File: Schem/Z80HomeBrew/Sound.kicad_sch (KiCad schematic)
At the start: 16 parts, among them J6 AudioJack3, U11 74HC00, U13 LM386, U18 SN76489AN, U8 SN76489AN, U9 74HC00

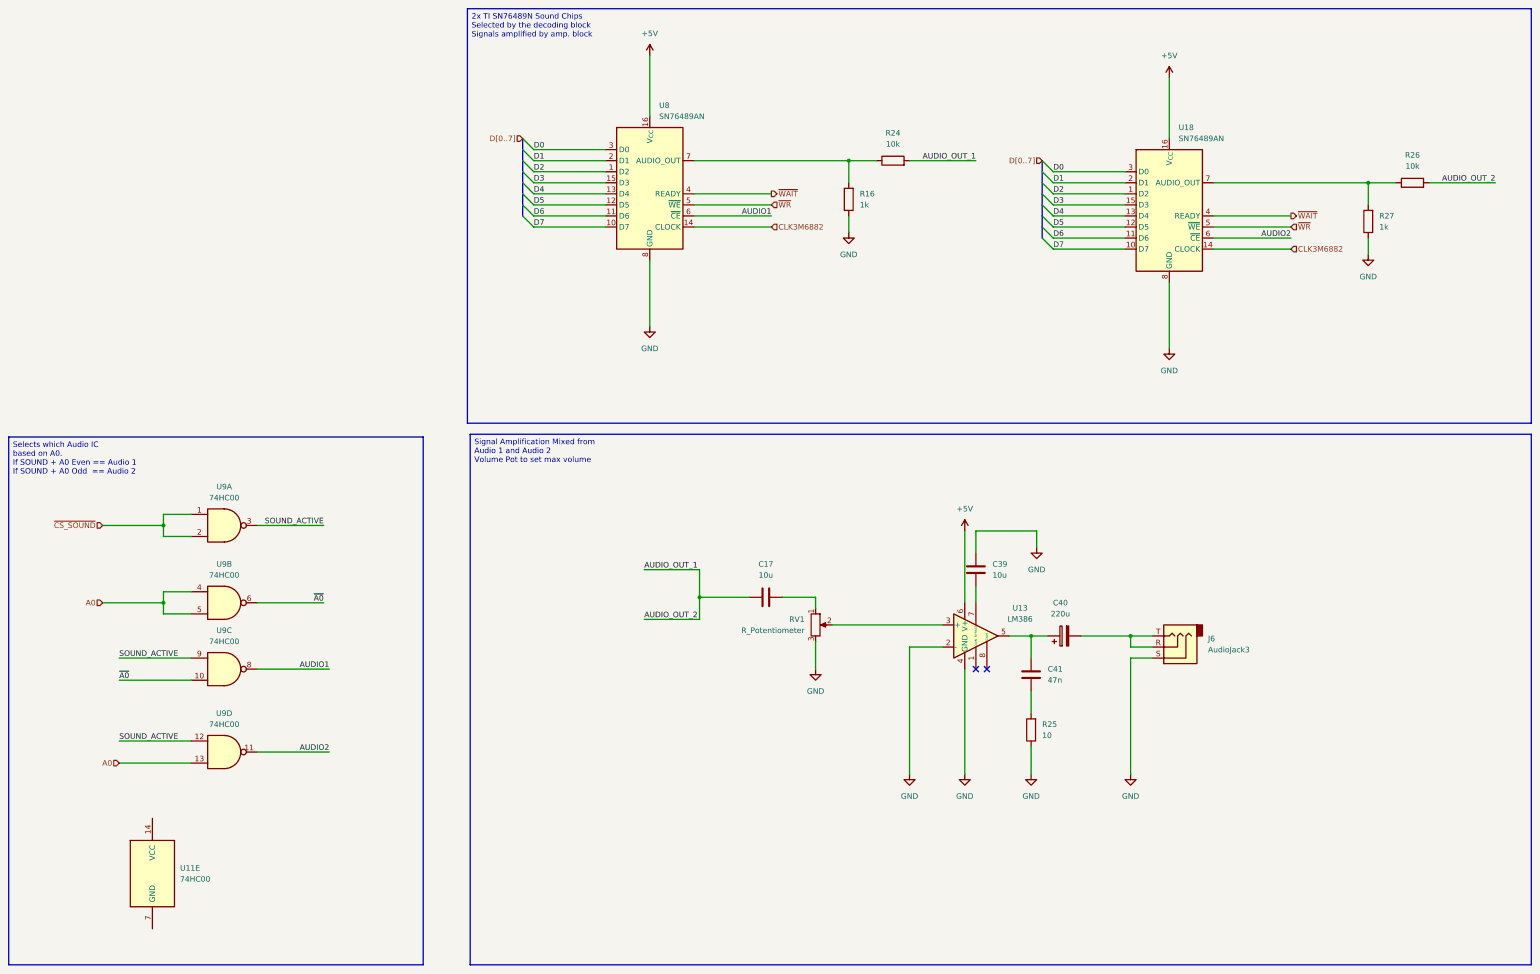
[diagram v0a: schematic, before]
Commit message: Video block added. fixed some issues with parts...
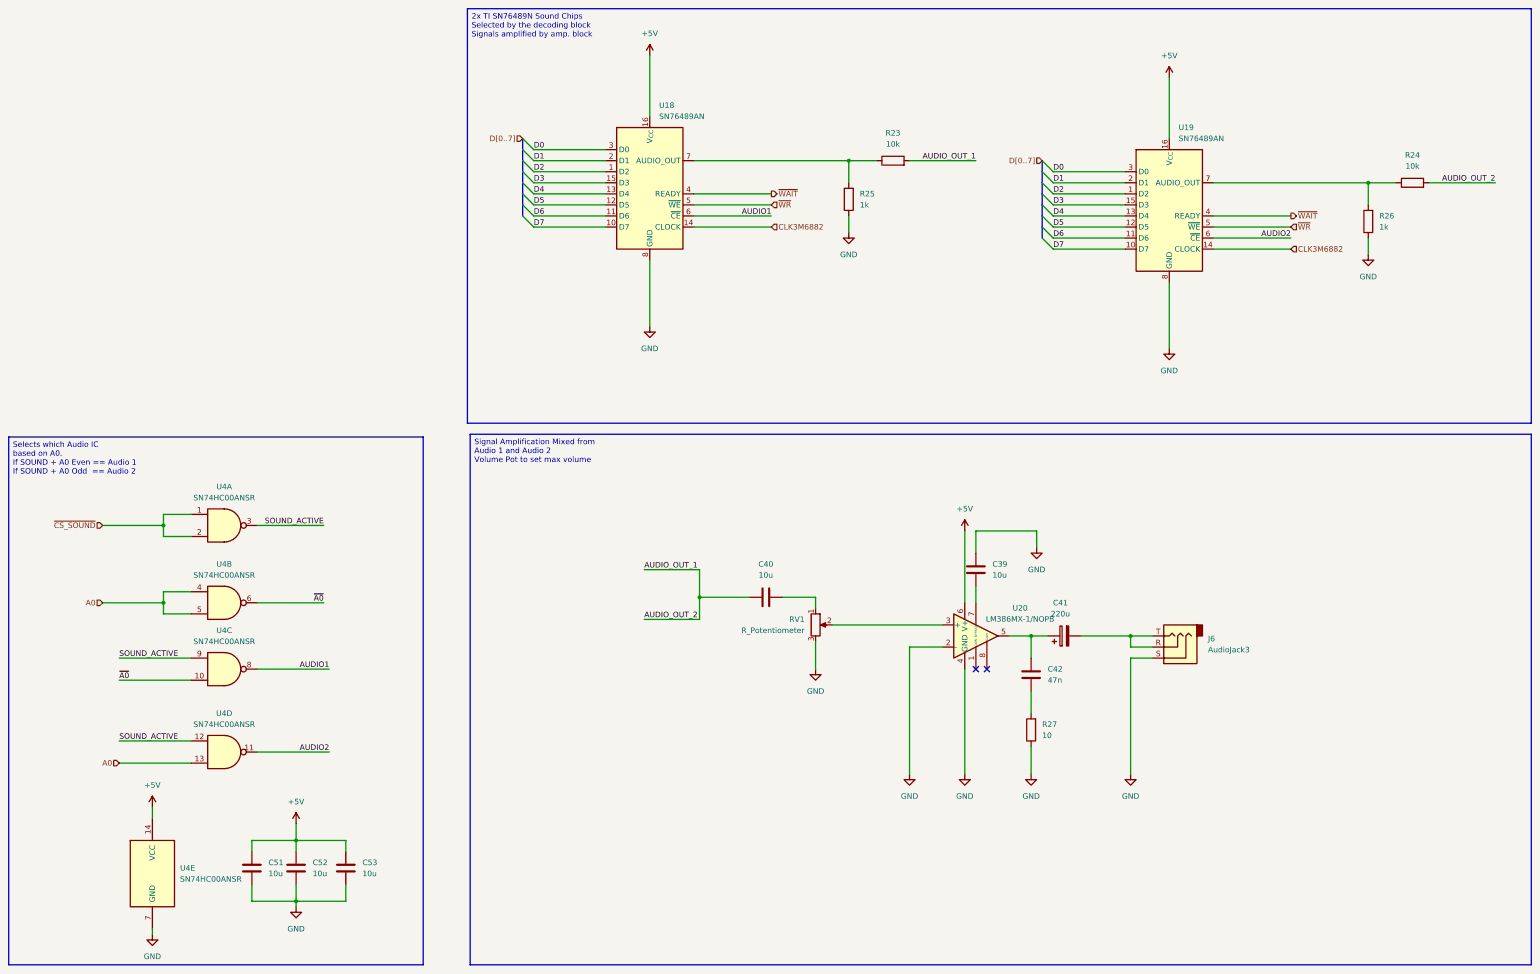
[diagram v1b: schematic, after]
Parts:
- added C51, C52, C53: 10u, Capacitor_SMD:C_1206_3216Metric, symbol Device:C
- U20: renamed from U13; value LM386 -> LM386MX-1/NOPB; footprint (none) -> Package_SO:SOIC-8_3.9x4.9mm_P1.27mm
- U4: renamed from U9; value 74HC00 -> SN74HC00ANSR; footprint (none) -> Footprints:SO14NB_TEX
- U4: renamed from U11; value 74HC00 -> SN74HC00ANSR; footprint (none) -> Footprints:SO14NB_TEX
- renumbered C17 to C40, C40 to C41, C41 to C42, R24 to R23, R26 to R24, R16 to R25, R27 to R26, R25 to R27, U8 to U18, U18 to U19
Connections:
- net +5V: now also U4.14 (VCC), C51.2, C52.2, C53.2
- net GND: now also U4.7 (GND), C51.1, C52.1, C53.1

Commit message: Completed schematics
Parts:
- J6: value AudioJack3 -> STX-3120-3B; footprint Connector_Audio:Jack_3.5mm_CUI_SJ1-3523N_Horizontal -> Footprints:KYCON_STX-3120-3B
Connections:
- net AUDIO_OUT_1 renamed AUDIO_OUT
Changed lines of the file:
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@@
 	(generator_version "9.0")
 	(paper "USLedger")
-	(text_box "Signal Amplification Mixed from\nAudio 1 and Audio 2\nVolume Pot to set max volume"
-		(exclude_from_sim no)
-		(at 128.905 121.285 0)
-		(size 243.84 121.92)
-		(margins 0.9525 0.9525 0.9525 0.9525)
-		(stroke
-			(width 0)
-			(type solid)
-		)
-		(fill
-			(type none)
-		)
-		(effects
-			(font
-				(size 1.27 1.27)
-			)
-			(justify left top)
-		)
-	)
 	(text_box "Selects which Audio IC\nbased on A0.\nIf SOUND + A0 Even == Audio 1\nIf SOUND + A0 Odd  == Audio 2"
 		(exclude_from_sim no)
@@
 	)
 	(junction
-		(at 181.61 158.75)
-		(diameter 0)
-		(color 0 0 0 0)
-	)
-	(junction
 		(at 280.67 167.64)
 		(diameter 0)
@@
 	(wire
 		(pts
-			(xy 168.91 152.4) (xy 181.61 152.4)
+			(xy 177.8 158.75) (xy 193.04 158.75)
 		)
 		(stroke
@@
 	(wire
 		(pts
-			(xy 181.61 158.75) (xy 181.61 152.4)
-		)
-		(stroke
-			(width 0)
-			(type default)
-		)
-	)
-	(wire
-		(pts
 			(xy 257.81 180.34) (xy 257.81 185.42)
 		)
@@
 	(wire
 		(pts
+			(xy 180.34 66.04) (xy 198.12 66.04)
+		)
+		(stroke
+			(width 0)
+			(type default)
+		)
+	)
+	(wire
+		(pts
 			(xy 44.45 142.24) (xy 58.42 142.24)
 		)
@@
 	(wire
 		(pts
-			(xy 168.91 163.83) (xy 181.61 163.83)
-		)
-		(stroke
-			(width 0)
-			(type default)
-		)
-	)
-	(wire
-		(pts
 			(xy 299.72 71.12) (xy 317.5 71.12)
 		)
@@
 	(wire
 		(pts
-			(xy 181.61 158.75) (xy 181.61 163.83)
-		)
-		(stroke
-			(width 0)
-			(type default)
-		)
-	)
-	(wire
-		(pts
 			(xy 299.72 78.74) (xy 317.5 78.74)
 		)
@@
 	(wire
 		(pts
-			(xy 181.61 158.75) (xy 193.04 158.75)
-		)
-		(stroke
-			(width 0)
-			(type default)
-		)
-	)
-	(wire
-		(pts
 			(xy 55.88 207.01) (xy 55.88 209.55)
 		)
@@
 		(pts
 			(xy 229.87 170.18) (xy 229.87 199.39)
-		)
-		(stroke
-			(width 0)
-			(type default)
-		)
-	)
-	(wire
-		(pts
-			(xy 180.34 66.04) (xy 198.12 66.04)
 		)
 		(stroke
@@
 		)
 	)
-	(label "AUDIO_OUT_1"
+	(label "AUDIO_OUT"
 		(at 245.11 58.42 180)
 		(effects
@@
 		)
 	)
-	(label "AUDIO_OUT_2"
-		(at 168.91 163.83 0)
-		(effects
-			(font
-				(size 1.27 1.27)
-			)
-			(justify left bottom)
-		)
-	)
 	(label "D3"
 		(at 262.89 68.58 0)
@@
 		)
 	)
-	(label "AUDIO_OUT_1"
-		(at 168.91 152.4 0)
+	(label "AUDIO_OUT"
+		(at 177.8 158.75 0)
 		(effects
 			(font
@@
 		)
 	)
-	(label "AUDIO_OUT_2"
+	(label "AUDIO_OUT"
 		(at 364.49 63.5 180)
 		(effects
@@
 	)
 	(hierarchical_label "~{WAIT}"
-		(shape output)
+		(shape tri_state)
 		(at 198.12 66.04 0)
 		(effects
@@
 	)
 	(hierarchical_label "~{WAIT}"
-		(shape output)
+		(shape tri_state)
 		(at 317.5 71.12 0)
 		(effects
@@
 			)
 		)
-		(property "Value" "AudioJack3"
+		(property "Value" "STX-3120-3B"
 			(at 298.45 170.8149 0)
 			(effects
@@
 			)
 		)
-		(property "Footprint" "Connector_Audio:Jack_3.5mm_CUI_SJ1-3523N_Horizontal"
+		(property "Footprint" "Footprints:KYCON_STX-3120-3B"
 			(at 290.83 170.18 0)
 			(effects

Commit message: Finally found a name "Zephyr-80" for the brew and committing the first pbc
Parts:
- added J13: Conn_01x03, Connector_PinSocket_2.54mm:PinSocket_1x03_P2.54mm_Vertical, symbol Connector_Generic:Conn_01x03
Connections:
- net A0: no longer U4.13
- net GND: now also J13.2 (Pin_2)
- net at C41.2, J6.R, J6.T: now also J13.1 (Pin_1), J13.3 (Pin_3)
- new net A1: U4.13
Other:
- note added: "Pin header as alternative to audio jack"
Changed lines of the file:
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@@
 	(generator_version "9.0")
 	(paper "USLedger")
+	(text "Pin header as alternative\nto audio jack"
+		(exclude_from_sim no)
+		(at 299.212 177.8 0)
+		(effects
+			(font
+				(size 1.27 1.27)
+			)
+		)
+	)
 	(text_box "Selects which Audio IC\nbased on A0.\nIf SOUND + A0 Even == Audio 1\nIf SOUND + A0 Odd  == Audio 2"
 		(exclude_from_sim no)
@@
 	)
 	(junction
+		(at 280.67 184.15)
+		(diameter 0)
+		(color 0 0 0 0)
+	)
+	(junction
 		(at 280.67 167.64)
 		(diameter 0)
@@
 	)
 	(junction
+		(at 284.48 170.18)
+		(diameter 0)
+		(color 0 0 0 0)
+	)
+	(junction
+		(at 283.21 167.64)
+		(diameter 0)
+		(color 0 0 0 0)
+	)
+	(junction
 		(at 257.81 167.64)
 		(diameter 0)
@@
 	(wire
 		(pts
-			(xy 280.67 170.18) (xy 285.75 170.18)
+			(xy 280.67 170.18) (xy 284.48 170.18)
 		)
 		(stroke
@@
 	(wire
 		(pts
+			(xy 280.67 184.15) (xy 280.67 199.39)
+		)
+		(stroke
+			(width 0)
+			(type default)
+		)
+	)
+	(wire
+		(pts
 			(xy 80.01 160.02) (xy 95.25 160.02)
 		)
@@
 	(wire
 		(pts
+			(xy 283.21 167.64) (xy 285.75 167.64)
+		)
+		(stroke
+			(width 0)
+			(type default)
+		)
+	)
+	(wire
+		(pts
 			(xy 262.89 63.5) (xy 279.4 63.5)
 		)
@@
 	(wire
 		(pts
+			(xy 280.67 172.72) (xy 285.75 172.72)
+		)
+		(stroke
+			(width 0)
+			(type default)
+		)
+	)
+	(wire
+		(pts
 			(xy 299.72 78.74) (xy 317.5 78.74)
 		)
@@
 	(wire
 		(pts
+			(xy 284.48 170.18) (xy 285.75 170.18)
+		)
+		(stroke
+			(width 0)
+			(type default)
+		)
+	)
+	(wire
+		(pts
 			(xy 78.74 228.6) (xy 88.9 228.6)
 		)
@@
 	(wire
 		(pts
+			(xy 288.29 186.69) (xy 283.21 186.69)
+		)
+		(stroke
+			(width 0)
+			(type default)
+		)
+	)
+	(wire
+		(pts
 			(xy 180.34 73.66) (xy 198.12 73.66)
 		)
@@
 	(wire
 		(pts
+			(xy 280.67 184.15) (xy 288.29 184.15)
+		)
+		(stroke
+			(width 0)
+			(type default)
+		)
+	)
+	(wire
+		(pts
 			(xy 237.49 170.18) (xy 229.87 170.18)
 		)
@@
 	(wire
 		(pts
-			(xy 280.67 167.64) (xy 285.75 167.64)
+			(xy 280.67 167.64) (xy 283.21 167.64)
 		)
 		(stroke
@@
 	(wire
 		(pts
-			(xy 280.67 172.72) (xy 280.67 199.39)
+			(xy 280.67 172.72) (xy 280.67 184.15)
 		)
 		(stroke
@@
 	(wire
 		(pts
+			(xy 284.48 170.18) (xy 284.48 181.61)
+		)
+		(stroke
+			(width 0)
+			(type default)
+		)
+	)
+	(wire
+		(pts
 			(xy 208.28 158.75) (xy 208.28 161.29)
 		)
@@
 	(wire
 		(pts
-			(xy 285.75 172.72) (xy 280.67 172.72)
-		)
-		(stroke
-			(width 0)
-			(type default)
-		)
-	)
-	(wire
-		(pts
 			(xy 245.11 156.21) (xy 245.11 160.02)
 		)
@@
 	(wire
 		(pts
+			(xy 288.29 181.61) (xy 284.48 181.61)
+		)
+		(stroke
+			(width 0)
+			(type default)
+		)
+	)
+	(wire
+		(pts
 			(xy 58.42 142.24) (xy 58.42 144.78)
+		)
+		(stroke
+			(width 0)
+			(type default)
+		)
+	)
+	(wire
+		(pts
+			(xy 283.21 186.69) (xy 283.21 167.64)
 		)
 		(stroke
@@
 		)
 	)
-	(hierarchical_label "A0"
+	(hierarchical_label "A1"
 		(shape input)
 		(at 48.26 196.85 180)
@@
 					(unit 1)
 				)
+			)
+		)
+	)
+	(symbol
+		(lib_id "Connector_Generic:Conn_01x03")
+		(at 293.37 184.15 0)
+		(unit 1)
+		(exclude_from_sim no)
+		(in_bom yes)
+		(on_board yes)
+		(dnp no)
+		(fields_autoplaced yes)
+		(property "Reference" "J13"
+			(at 295.91 182.8799 0)
+			(effects
+				(font
+					(size 1.27 1.27)
+				)
+				(justify left)
+			)
+		)
+		(property "Value" "Conn_01x03"
+			(at 295.91 185.4199 0)
+			(effects
+				(font
+					(size 1.27 1.27)
+				)
+				(justify left)
+			)
+		)
+		(property "Footprint" "Connector_PinSocket_2.54mm:PinSocket_1x03_P2.54mm_Vertical"
+			(at 293.37 184.15 0)
+			(effects
+				(font
+					(size 1.27 1.27)
+				)
+				(hide yes)
+			)
+		)
+		(property "Datasheet" "~"
+			(at 293.37 184.15 0)
+			(effects
+				(font
+					(size 1.27 1.27)
+				)
+				(hide yes)
+			)
+		)
+		(property "Description" "Generic connector, single row, 01x03, script generated (kicad-library-utils/schlib/autogen/connector/)"
+			(at 293.37 184.15 0)
+			(effects
+				(font
+					(size 1.27 1.27)
+				)
+				(hide yes)
+			)
+		)
+		(pin "1"
+		)
+		(pin "2"
+		)
+		(pin "3"
+		)
+		(instances
+			(project ""
+				(path "/5593e793-d133-45d0-a91e-72805049e474/8e76c343-c4fb-4794-ad0c-dd359d6b97e7"
+					(reference "J13")
+					(unit 1)
+				)
